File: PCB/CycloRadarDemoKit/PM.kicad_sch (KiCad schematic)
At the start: 1 part

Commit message: USB designed with TODOs, ESP part changed
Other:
- note added: "TODO: LEDs on every power line"
- note removed: "Notes: Max current from +5V_USB: 500mA"
- note removed: "TODO: LEDs on every line"
- moved on the sheet: R215
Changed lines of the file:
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@@
     (comment 1 "Designed by Martin Tavoda")
   )
-  (junction (at 93.98 41.91) (diameter 0) (color 0 0 0 0)
-  )
-  (wire (pts (xy 93.98 41.91) (xy 93.98 39.37))
+  (junction (at 93.98 36.83) (diameter 0) (color 0 0 0 0)
+  )
+  (wire (pts (xy 93.98 36.83) (xy 93.98 34.29))
     (stroke (width 0) (type default))
   )
@@
     (stroke (width 0) (type default))
   )
-  (wire (pts (xy 96.52 41.91) (xy 93.98 41.91))
-    (stroke (width 0) (type default))
-  )
-  (wire (pts (xy 83.82 41.91) (xy 85.09 41.91))
+  (wire (pts (xy 96.52 36.83) (xy 93.98 36.83))
+    (stroke (width 0) (type default))
+  )
+  (wire (pts (xy 83.82 36.83) (xy 85.09 36.83))
     (stroke (width 0) (type default))
   )
@@
     (stroke (width 0) (type default))
   )
-  (wire (pts (xy 96.52 39.37) (xy 96.52 41.91))
+  (wire (pts (xy 96.52 34.29) (xy 96.52 36.83))
     (stroke (width 0) (type default))
   )
@@
     (stroke (width 0) (type default))
   )
-  (wire (pts (xy 83.82 39.37) (xy 83.82 41.91))
+  (wire (pts (xy 83.82 34.29) (xy 83.82 36.83))
     (stroke (width 0) (type default))
   )
@@
     (stroke (width 0) (type default))
   )
-  (wire (pts (xy 92.71 41.91) (xy 93.98 41.91))
+  (wire (pts (xy 92.71 36.83) (xy 93.98 36.83))
     (stroke (width 0) (type default))
   )
@@
     (stroke (width 0) (type default))
   )
-  (text "Notes:\nMax current from +5V_USB: 500mA" (at 124.46 29.21 0)
+  (text "TODO: LEDs on every power line" (at 73.66 20.32 0)
     (effects (font (size 1.27 1.27)) (justify left bottom))
   )
-  (text "TODO: LEDs on every line" (at 73.66 20.32 0)
-    (effects (font (size 1.27 1.27)) (justify left bottom))
-  )
   (symbol (lib_id "power:+12V") (at 57.15 34.29 0) (unit 1)
     (in_bom yes) (on_board yes) (dnp no) (fields_autoplaced)
@@
     )
   )
-  (symbol (lib_id "power:+3V3_PHY") (at 93.98 39.37 0) (unit 1)
-    (in_bom yes) (on_board yes) (dnp no) (fields_autoplaced)
-    (property "Reference" "#PWR0216" (at 93.98 43.18 0)
-      (effects (font (size 1.27 1.27)) hide)
-    )
-    (property "Value" "+3V3_PHY" (at 93.98 34.29 0)
-      (effects (font (size 1.27 1.27)))
-    )
-    (property "Footprint" "" (at 93.98 39.37 0)
-      (effects (font (size 1.27 1.27)) hide)
-    )
-    (property "Datasheet" "" (at 93.98 39.37 0)
+  (symbol (lib_id "power:+3V3_PHY") (at 93.98 34.29 0) (unit 1)
+    (in_bom yes) (on_board yes) (dnp no) (fields_autoplaced)
+    (property "Reference" "#PWR0216" (at 93.98 38.1 0)
+      (effects (font (size 1.27 1.27)) hide)
+    )
+    (property "Value" "+3V3_PHY" (at 93.98 29.21 0)
+      (effects (font (size 1.27 1.27)))
+    )
+    (property "Footprint" "" (at 93.98 34.29 0)
+      (effects (font (size 1.27 1.27)) hide)
+    )
+    (property "Datasheet" "" (at 93.98 34.29 0)
       (effects (font (size 1.27 1.27)) hide)
     )
@@
     )
   )
-  (symbol (lib_name "+3V3_2") (lib_id "power:+3V3") (at 83.82 39.37 0) (unit 1)
-    (in_bom yes) (on_board yes) (dnp no) (fields_autoplaced)
-    (property "Reference" "#PWR0216" (at 83.82 43.18 0)
-      (effects (font (size 1.27 1.27)) hide)
-    )
-    (property "Value" "+3V3" (at 83.82 34.29 0)
-      (effects (font (size 1.27 1.27)))
-    )
-    (property "Footprint" "" (at 83.82 39.37 0)
-      (effects (font (size 1.27 1.27)) hide)
-    )
-    (property "Datasheet" "" (at 83.82 39.37 0)
+  (symbol (lib_name "+3V3_2") (lib_id "power:+3V3") (at 83.82 34.29 0) (unit 1)
+    (in_bom yes) (on_board yes) (dnp no) (fields_autoplaced)
+    (property "Reference" "#PWR0216" (at 83.82 38.1 0)
+      (effects (font (size 1.27 1.27)) hide)
+    )
+    (property "Value" "+3V3" (at 83.82 29.21 0)
+      (effects (font (size 1.27 1.27)))
+    )
+    (property "Footprint" "" (at 83.82 34.29 0)
+      (effects (font (size 1.27 1.27)) hide)
+    )
+    (property "Datasheet" "" (at 83.82 34.29 0)
       (effects (font (size 1.27 1.27)) hide)
     )
@@
     )
   )
-  (symbol (lib_id "power:PWR_FLAG") (at 96.52 39.37 0) (unit 1)
-    (in_bom yes) (on_board yes) (dnp no) (fields_autoplaced)
-    (property "Reference" "#FLG0404" (at 96.52 37.465 0)
-      (effects (font (size 1.27 1.27)) hide)
-    )
-    (property "Value" "PWR_FLAG" (at 96.52 34.29 0)
-      (effects (font (size 1.27 1.27)) hide)
-    )
-    (property "Footprint" "" (at 96.52 39.37 0)
-      (effects (font (size 1.27 1.27)) hide)
-    )
-    (property "Datasheet" "~" (at 96.52 39.37 0)
+  (symbol (lib_id "power:PWR_FLAG") (at 96.52 34.29 0) (unit 1)
+    (in_bom yes) (on_board yes) (dnp no) (fields_autoplaced)
+    (property "Reference" "#FLG0404" (at 96.52 32.385 0)
+      (effects (font (size 1.27 1.27)) hide)
+    )
+    (property "Value" "PWR_FLAG" (at 96.52 29.21 0)
+      (effects (font (size 1.27 1.27)) hide)
+    )
+    (property "Footprint" "" (at 96.52 34.29 0)
+      (effects (font (size 1.27 1.27)) hide)
+    )
+    (property "Datasheet" "~" (at 96.52 34.29 0)
       (effects (font (size 1.27 1.27)) hide)
     )
@@
     )
   )
-  (symbol (lib_id "Device:R") (at 88.9 41.91 90) (unit 1)
+  (symbol (lib_id "Device:R") (at 88.9 36.83 90) (unit 1)
     (in_bom yes) (on_board yes) (dnp no)
-    (property "Reference" "R215" (at 88.9 48.26 90)
-      (effects (font (size 1.27 1.27)))
-    )
-    (property "Value" "0R" (at 88.9 45.72 90)
-      (effects (font (size 1.27 1.27)))
-    )
-    (property "Footprint" "" (at 88.9 43.688 90)
-      (effects (font (size 1.27 1.27)) hide)
-    )
-    (property "Datasheet" "~" (at 88.9 41.91 0)
-      (effects (font (size 1.27 1.27)) hide)
-    )
+    (property "Reference" "R215" (at 88.9 43.18 90)
+      (effects (font (size 1.27 1.27)))
+    )
+    (property "Value" "0R" (at 88.9 40.64 90)
+      (effects (font (size 1.27 1.27)))
+    )
+    (property "Footprint" "" (at 88.9 38.608 90)
+      (effects (font (size 1.27 1.27)) hide)
+    )
+    (property "Datasheet" "~" (at 88.9 36.83 0)
+      (effects (font (size 1.27 1.27)) hide)
+    )

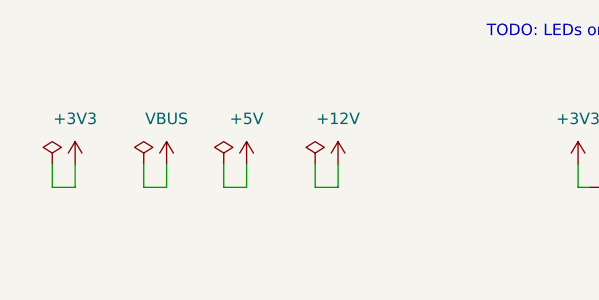
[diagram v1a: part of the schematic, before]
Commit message: Readme, PCB new symbol routed
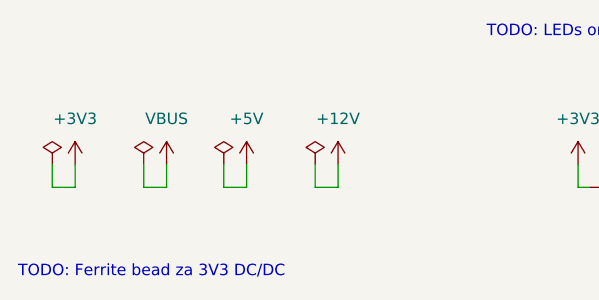
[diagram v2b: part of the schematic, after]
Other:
- note added: "TODO: Ferrite bead za 3V3 DC/DC"
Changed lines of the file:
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@@
     (stroke (width 0) (type default))
+  )
+  (text "TODO: Ferrite bead za 3V3 DC/DC" (at 21.59 46.99 0)
+    (effects (font (size 1.27 1.27)) (justify left bottom))
   )
   (text "TODO: LEDs on every power line" (at 73.66 20.32 0)

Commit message: PCB power manag. WIP
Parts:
- added C401: 10uF/25V(10%), Capacitor_SMD:C_1206_3216Metric, symbol Device:C_Small
- added C402: 10nF/50V(10%), Capacitor_SMD:C_0603_1608Metric, symbol Device:C_Small
- added C403: 22uF/16V(20%), Capacitor_SMD:C_1206_3216Metric, symbol Device:C_Small
- added D401: D_Schottky, symbol Device:D_Schottky
- added J401: 20-16V Supply Voltage, symbol Connector_Generic:Conn_01x02
- added L401: 15uH/1A, symbol Device:L
- added Q401: SI2309CDS, symbol Simulation_SPICE:PMOS
- added R215: 0R, Resistor_SMD:R_0603_1608Metric, symbol Device:R
- added R403: 51K(1%), Resistor_SMD:R_0603_1608Metric, symbol Device:R
- added R404: 3.6K(1%), Resistor_SMD:R_0603_1608Metric, symbol Device:R
- added R405: 0.2R(1%), Resistor_SMD:R_2010_5025Metric, symbol Device:R_Shunt
- added R406: R_Shunt, Resistor_SMD:R_2010_5025Metric, symbol Device:R_Shunt
- added U402: RT8259, Package_TO_SOT_SMD:TSOT-23-6, symbol Regulator_Switching:RT8259
- R215: footprint (none) -> Resistor_SMD:R_0603_1608Metric
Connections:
- net +12V: now also R215.2
- new net: J401.2 (Pin_2), Q401.1 (D)
- new net: Q401.2 (G), Q401.3 (S), R405.1
- new net: C402.1, U402.1 (BOOT)
- new net: R403.2, R404.1, U402.3 (FB)
- new net: C401.1, R405.2, U402.5 (VIN)
- new net: C402.2, D401.1 (K), L401.1, U402.6 (PHASE)
- new net: C403.2, L401.2, R403.1, R406.2
- new net: R215.1, R406.1
- new net 12V_EN: U402.4 (EN)
- new net GND: C401.2, C403.1, D401.2 (A), J401.1 (Pin_1), R404.2, U402.2 (GND)
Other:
- note added: "Battery pack 3.7*5 = 18.5V => max 20V 3.2*5 = 16V"
- note added: "Maximum power values: CP2102N 3V3 10mA (USB) ESP32 3V3 500mA MPU 3V3 4mA D52 ANT 3V3 20mA IP101 PHY 3V3 500mA PMICs 3.3V 0.5mA + 0.4mA + 0.03mA + 0.3mA = 1.3mA RESERVE: 200mA 3V3 1.23A = 4W -> (94%)@4.24W LEDs 5V 240mA = 1.2W + 4.24W -> (87%)@6.1472W Radar 12V 500mA = 6W -> (90%)@6.6W 12.75W -> 20V @ 640mA 16.5V @ 772mA"
- note added: "f = 1.4MHZ"

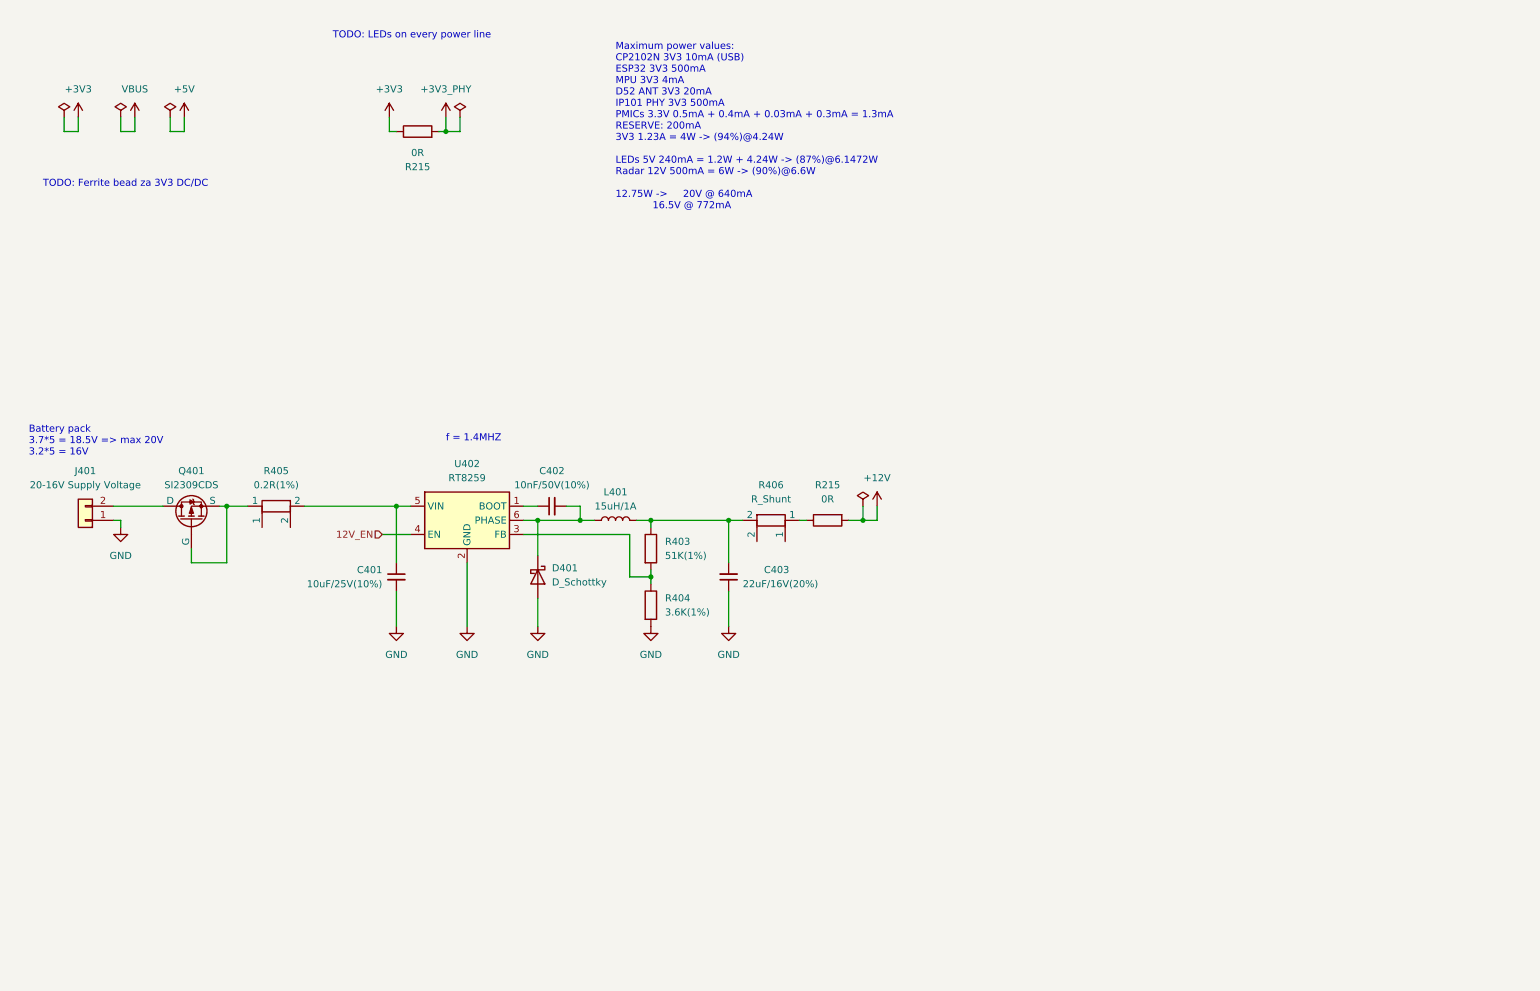
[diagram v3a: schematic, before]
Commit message: Power management almost done
5V/3.3V changed to AP63203
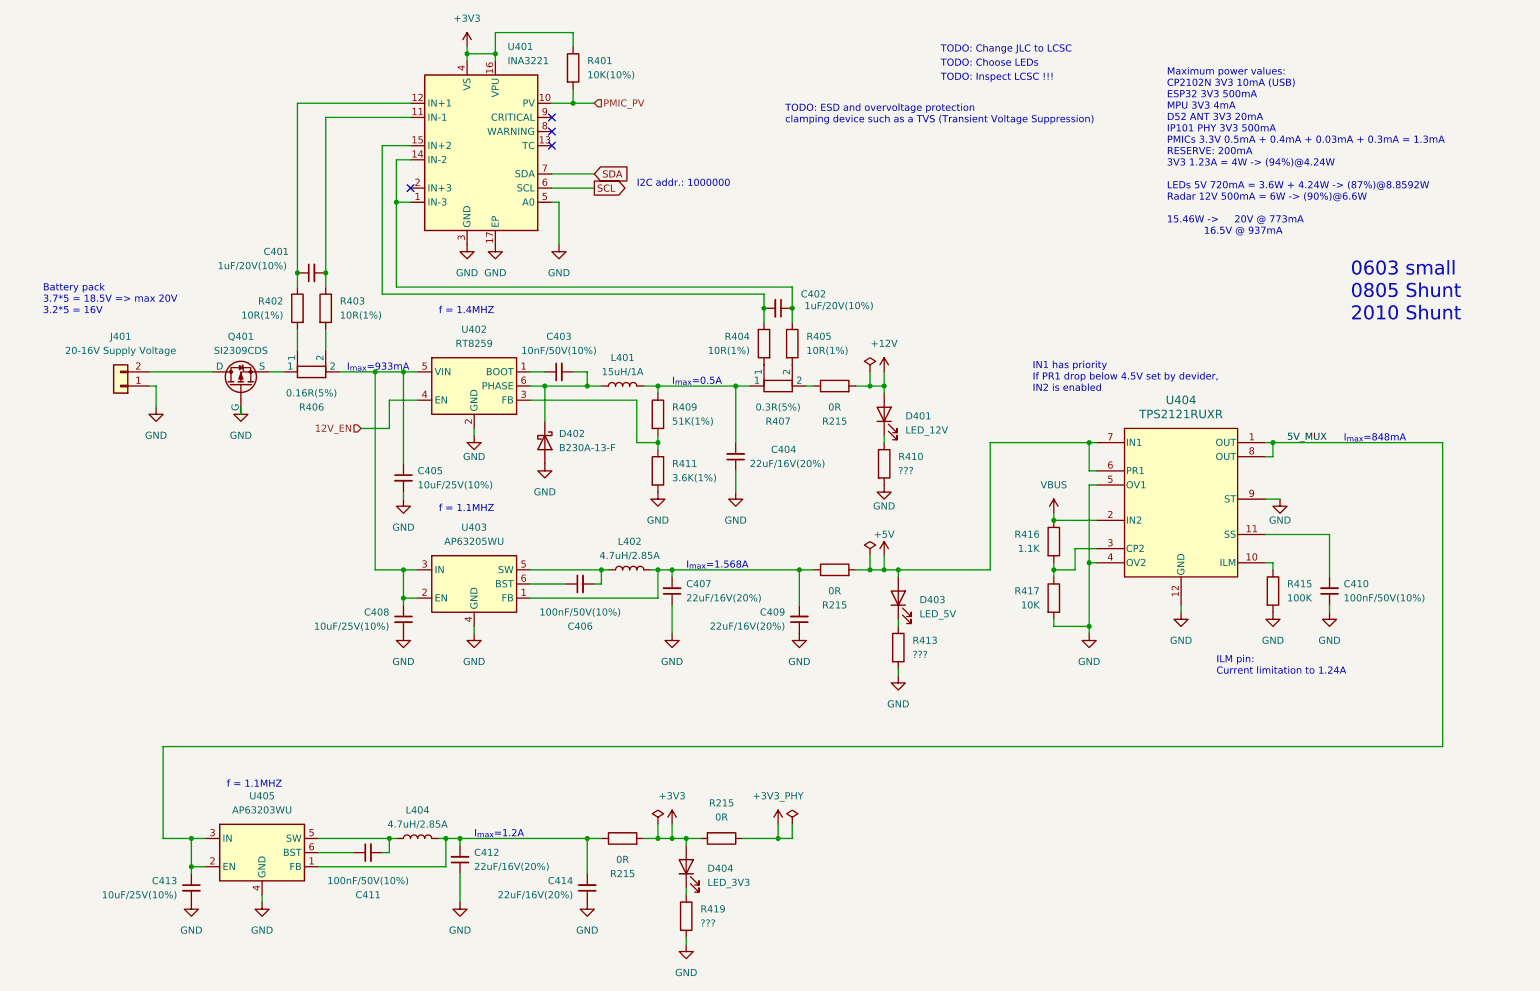
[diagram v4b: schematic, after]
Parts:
- removed R406: R_Shunt, Resistor_SMD:R_2010_5025Metric, symbol Device:R_Shunt
- added C401, C402: 1uF/20V(10%), Capacitor_SMD:C_0603_1608Metric, symbol Device:C_Small
- added C406, C410, C411: 100nF/50V(10%), Capacitor_SMD:C_0805_2012Metric, symbol Device:C_Small
- added C407, C409, C412, C414: 22uF/16V(20%), Capacitor_SMD:C_1206_3216Metric, symbol Device:C_Small
- added C408, C413: 10uF/25V(10%), Capacitor_SMD:C_1206_3216Metric, symbol Device:C_Small
- added D401: LED_12V, symbol Device:LED
- added D403: LED_5V, symbol Device:LED
- added D404: LED_3V3, symbol Device:LED
- added L402, L404: 4.7uH/2.85A, Inductor_SMD:L_Sunlord_SWPA4020S, symbol Device:L
- added R215 (x2): 0R, symbol Device:R
- added R401: 10K(10%), symbol Device:R
- added R402, R403, R404, R405: 10R(1%), Resistor_SMD:R_0603_1608Metric, symbol Device:R
- added R407: 0.3R(5%), Resistor_SMD:R_0805_2012Metric, symbol Device:R_Shunt
- added R410, R413, R419: ???, symbol Device:R
- added R415: 100K, symbol Device:R
- added R416: 1.1K, symbol Device:R
- added R417: 10K, symbol Device:R
- added U401: INA3221, Package_DFN_QFN:Texas_RGV_S-PVQFN-N16_EP2.1x2.1mm, symbol Power_Management:INA3221
- added U403: AP63205WU, Package_TO_SOT_SMD:TSOT-23-6, symbol Regulator_Switching:AP63205WU
- added U404: TPS2121RUXR, TPS2121:TPS2121, symbol TPS2121:TPS2121RUXR
- added U405: AP63203WU, Package_TO_SOT_SMD:TSOT-23-6, symbol Regulator_Switching:AP63205WU
- C403: renamed from C402; JLC C57112 -> (none); LCSC (none) -> C57112
- C404: renamed from C403; JLC C87162 -> (none); LCSC (none) -> C87162
- C405: renamed from C401; JLC C77090 -> (none); LCSC (none) -> C77090
- D402: renamed from D401; value D_Schottky -> B230A-13-F; footprint (none) -> Diode_SMD:D_SMA; LCSC (none) -> C12889
- L401: JLC C167809 -> (none); LCSC (none) -> C167809
- Q401: footprint (none) -> Package_TO_SOT_SMD:SOT-23; JLC C3021112 -> (none); LCSC (none) -> C3021112
- R215: footprint Resistor_SMD:R_0603_1608Metric -> (none)
- R406: renamed from R405; value 0.2R(1%) -> 0.16R(5%); footprint Resistor_SMD:R_2010_5025Metric -> Resistor_SMD:R_1210_3225Metric; JLC C2145167 -> (none); LCSC (none) -> C175910; Power 750mW -> 500mW
- R409: renamed from R403; JLC C23196 -> (none); LCSC (none) -> C23196
- R411: renamed from R404; JLC C22980 -> (none); LCSC (none) -> C22980
- U402: JLC C425775 -> (none); LCSC (none) -> C425775
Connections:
- net +12V: now also D401.2 (A)
- net +3V3: now also R215.2, D404.2 (A), R215.2, R401.1, U401.16 (VPU), U401.4 (VS); no longer R215.1
- net +3V3_PHY: now also R215.1; no longer R215.2
- net +5V: now also D403.2 (A), R215.2, U404.6 (PR1), U404.7 (IN1)
- net GND: now also Q401.2 (G), C407.1, C408.2, C409.1, C410.1, C412.1, C413.2, C414.1, R410.2, R413.2, R415.2, R417.2, R419.2, U401.17 (EP), U401.3 (GND), U401.5 (A0), U403.4 (GND), U404.12 (GND), U404.4 (OV2), U404.5 (OV1), U404.9 (ST), U405.4 (GND)
- net VBUS: now also R416.1, U404.2 (IN2)
- net at C405.1, R406.2, U402.5 (VIN): now also C408.1, U403.2 (EN), U403.3 (IN)
- net at R406.1: now also R402.2
- net at R406.2: now also R403.2
- net at C404.2, L401.2, R409.1: now also R407.1
- net at R215.1: now also R407.2
- new net: C402.1, R405.1, U401.1 (IN-3), U401.14 (IN-2)
- new net: C401.2, R403.1, U401.11 (IN-1)
- new net: C401.1, R402.1, U401.12 (IN+1)
- new net: C402.2, R404.1, U401.15 (IN+2)
- new net: D401.1 (K), R410.1
- new net: C407.2, C409.2, L402.2, R215.1, U403.1 (FB)
- new net: Q401.3 (S), R406.1
- new net: D404.1 (K), R419.1
- new net: R404.2, R407.1
- new net: R415.1, U404.10 (ILM)
- new net: C410.2, U404.11 (SS)
- new net: R416.2, R417.1, U404.3 (CP2)
- new net: C411.1, U405.6 (BST)
- new net: C411.2, L404.1, U405.5 (SW)
- new net: C412.2, C414.2, L404.2, R215.1, U405.1 (FB)
- new net: D403.1 (K), R413.1
- new net: C406.2, L402.1, U403.5 (SW)
- new net: C406.1, U403.6 (BST)
- new net: R405.2, R407.2
- new net 5V_MUX: C413.1, U404.1 (OUT), U404.8 (OUT), U405.2 (EN), U405.3 (IN)
- new net PMIC_PV: R401.2, U401.10 (PV)
- new net SCL: U401.6 (SCL)
- new net SDA: U401.7 (SDA)
- no-connect marks 0 -> 4
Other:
- note added: "0603 small 0805 Shunt 2010 Shunt"
- note added: "I2C addr.: 1000000"
- note added: "ILM pin: Current limitation to 1.24A"
- note added: "IN1 has priority If PR1 drop below 4.5V set by devider, IN2 is enabled"
- note added: "I_{max}=0.5A"
- note added: "I_{max}=1.2A"
- note added: "I_{max}=1.568A"
- note added: "I_{max}=848mA"
- note added: "I_{max}=933mA"
- note added: "Maximum power values: CP2102N 3V3 10mA (USB) ESP32 3V3 500mA MPU 3V3 4mA D52 ANT 3V3 20mA IP101 PHY 3V3 500mA PMICs 3.3V 0.5mA + 0.4mA + 0.03mA + 0.3mA = 1.3mA RESERVE: 200mA 3V3 1.23A = 4W -> (94%)@4.24W LEDs 5V 720mA = 3.6W + 4.24W -> (87%)@8.8592W Radar 12V 500mA = 6W -> (90%)@6.6W 15.46W -> 20V @ 773mA 16.5V @ 937mA"
- note added: "TODO: Change JLC to LCSC"
- note added: "TODO: Choose LEDs"
- note added: "TODO: ESD and overvoltage protection clamping device such as a TVS (Transient Voltage Suppression)"
- note added: "TODO: Inspect LCSC !!!"
- note added: "f = 1.1MHZ"
- note removed: "Maximum power values: CP2102N 3V3 10mA (USB) ESP32 3V3 500mA MPU 3V3 4mA D52 ANT 3V3 20mA IP101 PHY 3V3 500mA PMICs 3.3V 0.5mA + 0.4mA + 0.03mA + 0.3mA = 1.3mA RESERVE: 200mA 3V3 1.23A = 4W -> (94%)@4.24W LEDs 5V 240mA = 1.2W + 4.24W -> (87%)@6.1472W Radar 12V 500mA = 6W -> (90%)@6.6W 12.75W -> 20V @ 640mA 16.5V @ 772mA"
- note removed: "TODO: Ferrite bead za 3V3 DC/DC"
- note removed: "TODO: LEDs on every power line"
- moved on the sheet: C403, C404, C405, D402, J401, L401, Q401, R215, R406, R409, R411, U402

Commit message: RJ45 chose, leds connected
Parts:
- C401, C402: value 1uF/20V(10%) -> 1uF/50V(10%); LCSC (none) -> C15849
- R215: footprint (none) -> Resistor_SMD:R_0805_2012Metric; LCSC (none) -> C17477
- R402, R403, R404, R405: footprint Resistor_SMD:R_0603_1608Metric -> (none)
- U401: LCSC (none) -> C181255
- U403: renamed from U404; LCSC (none) -> C485916
- renumbered C410 to C408, C408 to C409, C409 to C410, L404 to L403, R416 to R412, R415 to R414, R417 to R415, R413 to R416, U403 to U404

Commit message: MCU routed, two GPIO tested
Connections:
- net 12V_EN renamed 12V_DIS
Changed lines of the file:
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@@
     (effects (font (size 1.27 1.27)) (justify left bottom))
   )
-  (global_label "SDA" (shape input) (at 120.65 44.45 0) (fields_autoplaced)
+  (global_label "SDA" (shape bidirectional) (at 120.65 44.45 0) (fields_autoplaced)
     (effects (font (size 1.27 1.27)) (justify left))
-    (property "Intersheetrefs" "${INTERSHEET_REFS}" (at 127.2033 44.45 0)
+    (property "Intersheetrefs" "${INTERSHEET_REFS}" (at 128.3146 44.45 0)
       (effects (font (size 1.27 1.27)) (justify left) hide)
     )
   )
-  (global_label "SCL" (shape output) (at 120.65 46.99 0) (fields_autoplaced)
+  (global_label "SCL" (shape input) (at 120.65 46.99 0) (fields_autoplaced)
     (effects (font (size 1.27 1.27)) (justify left))
     (property "Intersheetrefs" "${INTERSHEET_REFS}" (at 127.1428 46.99 0)
@@
     )
   )
-  (hierarchical_label "12V_EN" (shape input) (at 78.74 90.17 180) (fields_autoplaced)
+  (hierarchical_label "12V_DIS" (shape input) (at 78.74 90.17 180) (fields_autoplaced)
     (effects (font (size 1.27 1.27)) (justify right))
   )
